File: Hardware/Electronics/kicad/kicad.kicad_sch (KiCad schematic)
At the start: 53 parts, among them J4 Conn_01x04, J5 Conn_01x04, J6 USB_C_Receptacle_USB2.0_16P, J7 Conn_01x04, SW1 SW_Push, SW2 SW_Push, SW3 SW_Push, U1 USBLC6-2P6, U10 SN74LV1T34DBV, U2 MCP73831-2-OT, U3 ESP32-C3-MINI-1-N4, U4 XC6210B332MR, U5 TPS61023DRLR, U6 SN74LV1T34DBV, U7 FPC-0.5HF-8PWBH10, U8 FPC-0.5HF-8PWBH10, U9 FPC-0.5HF-8PWBH10

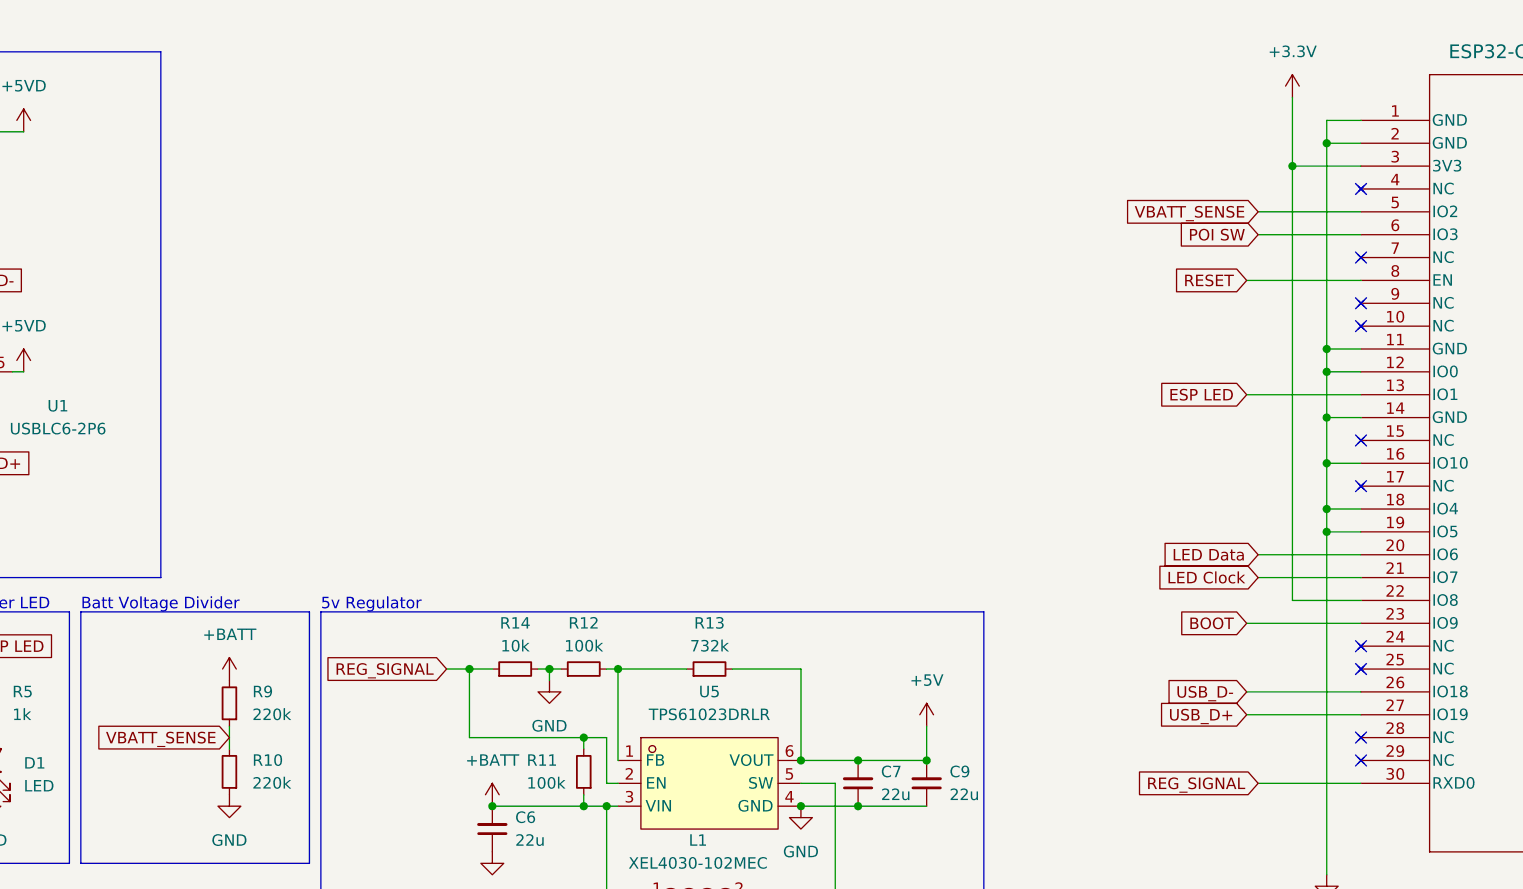
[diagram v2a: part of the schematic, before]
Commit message: Add pullup to gpio8, change board "version" to 3.0.0 due to new data pinout.
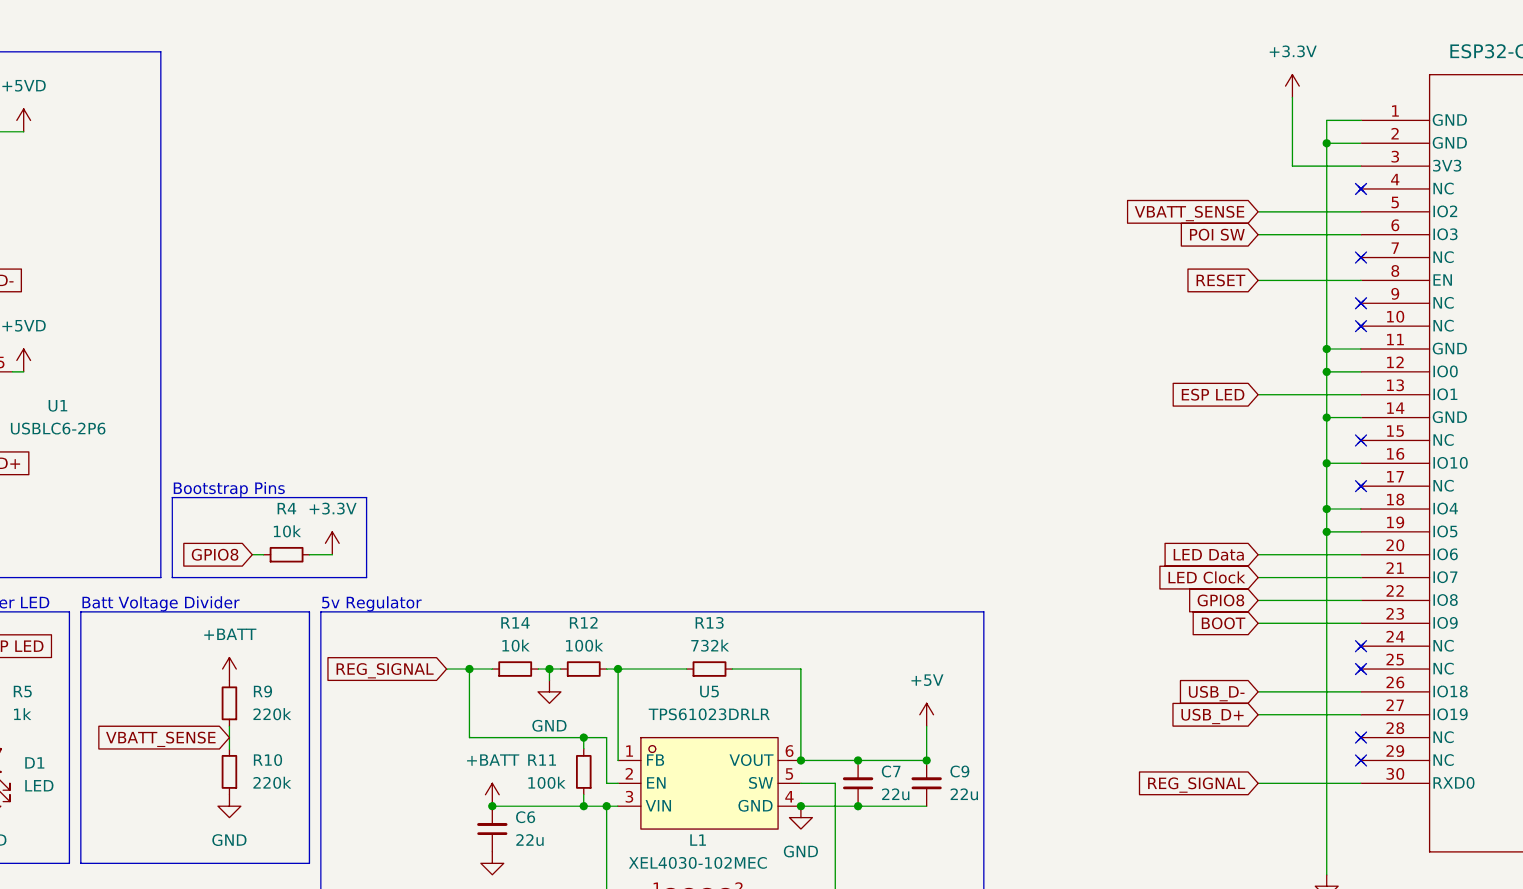
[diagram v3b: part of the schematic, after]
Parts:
- added R4: 10k, Resistor_SMD:R_0603_1608Metric, symbol Device:R_Small
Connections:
- net +3.3V: now also R4.2; no longer U3.22 (IO8)
- new net GPIO8: R4.1, U3.22 (IO8)
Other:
- note added: "Bootstrap Pins"
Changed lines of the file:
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@@
   (junction (at 184.15 137.16) (diameter 0) (color 0 0 0 0)
-  )
-  (junction (at 210.82 31.75) (diameter 0) (color 0 0 0 0)
   )
   (junction (at 119.38 87.63) (diameter 0) (color 0 0 0 0)
@@
     (stroke (width 0) (type default))
   )
-  (wire (pts (xy 205.74 44.45) (xy 218.44 44.45))
+  (wire (pts (xy 207.01 44.45) (xy 218.44 44.45))
     (stroke (width 0) (type default))
   )
@@
     (stroke (width 0) (type default))
   )
+  (wire (pts (xy 96.52 74.93) (xy 95.25 74.93))
+    (stroke (width 0) (type default))
+  )
   (wire (pts (xy 259.08 41.91) (xy 262.89 41.91))
     (stroke (width 0) (type default))
@@
     (stroke (width 0) (type default))
   )
-  (wire (pts (xy 205.74 57.15) (xy 218.44 57.15))
+  (wire (pts (xy 207.01 57.15) (xy 218.44 57.15))
     (stroke (width 0) (type default))
   )
@@
     (stroke (width 0) (type default))
   )
-  (wire (pts (xy 205.74 90.17) (xy 218.44 90.17))
+  (wire (pts (xy 207.01 90.17) (xy 218.44 90.17))
     (stroke (width 0) (type default))
   )
@@
     (stroke (width 0) (type default))
   )
+  (wire (pts (xy 207.01 82.55) (xy 218.44 82.55))
+    (stroke (width 0) (type default))
+  )
   (wire (pts (xy 214.63 26.67) (xy 214.63 29.21))
     (stroke (width 0) (type default))
@@
     (stroke (width 0) (type default))
   )
+  (wire (pts (xy 101.6 74.93) (xy 104.14 74.93))
+    (stroke (width 0) (type default))
+  )
   (wire (pts (xy 259.08 39.37) (xy 262.89 39.37))
     (stroke (width 0) (type default))
@@
     (stroke (width 0) (type default))
   )
-  (wire (pts (xy 218.44 80.01) (xy 210.82 80.01))
-    (stroke (width 0) (type default))
-  )
   (wire (pts (xy 218.44 26.67) (xy 214.63 26.67))
     (stroke (width 0) (type default))
@@
     (stroke (width 0) (type default))
   )
-  (wire (pts (xy 210.82 80.01) (xy 210.82 31.75))
-    (stroke (width 0) (type default))
-  )
   (wire (pts (xy 184.15 137.16) (xy 176.53 137.16))
     (stroke (width 0) (type default))
@@
     (stroke (width 0) (type default))
   )
+  (wire (pts (xy 207.01 80.01) (xy 218.44 80.01))
+    (stroke (width 0) (type default))
+  )
   (wire (pts (xy 214.63 54.61) (xy 214.63 59.69))
     (stroke (width 0) (type default))
@@
     (stroke (width 0) (type default))
   )
-  (wire (pts (xy 205.74 92.71) (xy 218.44 92.71))
+  (wire (pts (xy 207.01 92.71) (xy 218.44 92.71))
     (stroke (width 0) (type default))
   )
@@
     (stroke (width 0) (type default))
   )
-  (wire (pts (xy 205.74 82.55) (xy 218.44 82.55))
-    (stroke (width 0) (type default))
-  )
   (wire (pts (xy 27.94 102.87) (xy 29.21 102.87))
     (stroke (width 0) (type default))
@@
   )
   (rectangle (start 152.4 118.11) (end 189.23 167.64)
+    (stroke (width 0) (type default))
+    (fill (type none))
+  )
+  (rectangle (start 86.36 68.58) (end 107.95 77.47)
     (stroke (width 0) (type default))
     (fill (type none))
@@
   )
   (text "ESP Power LED" (at 59.69 81.28 0)
+    (effects (font (size 1.27 1.27)) (justify left bottom))
+  )
+  (text "Bootstrap Pins" (at 86.36 68.58 0)
     (effects (font (size 1.27 1.27)) (justify left bottom))
   )
@@
     )
   )
-  (global_label "ESP LED" (shape input) (at 205.74 57.15 180) (fields_autoplaced)
+  (global_label "ESP LED" (shape input) (at 207.01 57.15 180) (fields_autoplaced)
     (effects (font (size 1.27 1.27)) (justify right))
-    (property "Intersheetrefs" "${INTERSHEET_REFS}" (at 194.7116 57.15 0)
+    (property "Intersheetrefs" "${INTERSHEET_REFS}" (at 195.9816 57.15 0)
+      (effects (font (size 1.27 1.27)) (justify right) hide)
+    )
+  )
+  (global_label "GPIO8" (shape input) (at 207.01 80.01 180) (fields_autoplaced)
+    (effects (font (size 1.27 1.27)) (justify right))
+    (property "Intersheetrefs" "${INTERSHEET_REFS}" (at 198.34 80.01 0)
       (effects (font (size 1.27 1.27)) (justify right) hide)
     )
@@
     )
   )
-  (global_label "USB_D+" (shape input) (at 205.74 92.71 180) (fields_autoplaced)
+  (global_label "GPIO8" (shape input) (at 95.25 74.93 180) (fields_autoplaced)
     (effects (font (size 1.27 1.27)) (justify right))
-    (property "Intersheetrefs" "${INTERSHEET_REFS}" (at 195.1348 92.71 0)
+    (property "Intersheetrefs" "${INTERSHEET_REFS}" (at 86.58 74.93 0)
+      (effects (font (size 1.27 1.27)) (justify right) hide)
+    )
+  )
+  (global_label "USB_D+" (shape input) (at 207.01 92.71 180) (fields_autoplaced)
+    (effects (font (size 1.27 1.27)) (justify right))
+    (property "Intersheetrefs" "${INTERSHEET_REFS}" (at 196.4048 92.71 0)
       (effects (font (size 1.27 1.27)) (justify right) hide)
     )
@@
     )
   )
-  (global_label "BOOT" (shape input) (at 205.74 82.55 180) (fields_autoplaced)
+  (global_label "BOOT" (shape input) (at 207.01 82.55 180) (fields_autoplaced)
     (effects (font (size 1.27 1.27)) (justify right))
-    (property "Intersheetrefs" "${INTERSHEET_REFS}" (at 197.8562 82.55 0)
+    (property "Intersheetrefs" "${INTERSHEET_REFS}" (at 199.1262 82.55 0)
       (effects (font (size 1.27 1.27)) (justify right) hide)
     )
   )
-  (global_label "RESET" (shape input) (at 205.74 44.45 180) (fields_autoplaced)
+  (global_label "RESET" (shape input) (at 207.01 44.45 180) (fields_autoplaced)
     (effects (font (size 1.27 1.27)) (justify right))
-    (property "Intersheetrefs" "${INTERSHEET_REFS}" (at 197.0097 44.45 0)
+    (property "Intersheetrefs" "${INTERSHEET_REFS}" (at 198.2797 44.45 0)
       (effects (font (size 1.27 1.27)) (justify right) hide)
     )
@@
     )
   )
-  (global_label "USB_D-" (shape input) (at 205.74 90.17 180) (fields_autoplaced)
+  (global_label "USB_D-" (shape input) (at 207.01 90.17 180) (fields_autoplaced)
     (effects (font (size 1.27 1.27)) (justify right))
-    (property "Intersheetrefs" "${INTERSHEET_REFS}" (at 195.1348 90.17 0)
+    (property "Intersheetrefs" "${INTERSHEET_REFS}" (at 196.4048 90.17 0)
       (effects (font (size 1.27 1.27)) (justify right) hide)
     )
@@
     )
   )
+  (symbol (lib_id "Device:R_Small") (at 99.06 74.93 90) (unit 1)
+    (in_bom yes) (on_board yes) (dnp no) (fields_autoplaced)
+    (property "Reference" "R4" (at 99.06 69.85 90)
+      (effects (font (size 1.27 1.27)))
+    )
+    (property "Value" "10k" (at 99.06 72.39 90)
+      (effects (font (size 1.27 1.27)))
+    )
+    (property "Footprint" "Resistor_SMD:R_0603_1608Metric" (at 99.06 74.93 0)
+      (effects (font (size 1.27 1.27)) hide)
+    )
+    (property "Datasheet" "~" (at 99.06 74.93 0)
+      (effects (font (size 1.27 1.27)) hide)
+    )
+    (property "LCSC" "C98220" (at 99.06 74.93 0)
+      (effects (font (size 1.27 1.27)) hide)
+    )
+    (pin "1")
+    (pin "2")
+    (instances
+      (project "kicad"
+        (path "/55a1363e-3506-4b1f-a7a5-0f5495c7c793"
+          (reference "R4") (unit 1)
+        )
+      )
+    )
+  )
   (symbol (lib_id "power:GND") (at 48.26 54.61 0) (unit 1)
     (in_bom yes) (on_board yes) (dnp no)
@@
         )
       )
+    )
+  )
+  (symbol (lib_id "power:+3.3V") (at 104.14 74.93 0) (unit 1)
+    (in_bom yes) (on_board yes) (dnp no) (fields_autoplaced)
+    (property "Reference" "#PWR038" (at 104.14 78.74 0)
+      (effects (font (size 1.27 1.27)) hide)
+    )
+    (property "Value" "+3.3V" (at 104.14 69.85 0)
+      (effects (font (size 1.27 1.27)))
+    )
+    (property "Footprint" "" (at 104.14 74.93 0)
+      (effects (font (size 1.27 1.27)) hide)
+    )
+    (property "Datasheet" "" (at 104.14 74.93 0)
+      (effects (font (size 1.27 1.27)) hide)
+    )
+    (pin "1")
+    (instances
+      (project "kicad"
+        (path "/55a1363e-3506-4b1f-a7a5-0f5495c7c793"
+          (reference "#PWR038") (unit 1)
+        )
+      )
